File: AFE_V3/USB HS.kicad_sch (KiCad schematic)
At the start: 29 parts, among them IC16 USB3300-EZK-TR, IC17 STMPS2151MTR, J2 USB_C_Receptacle_USB2.0_16P, U8 USBLC6-2SC6, Y1 Crystal_GND24

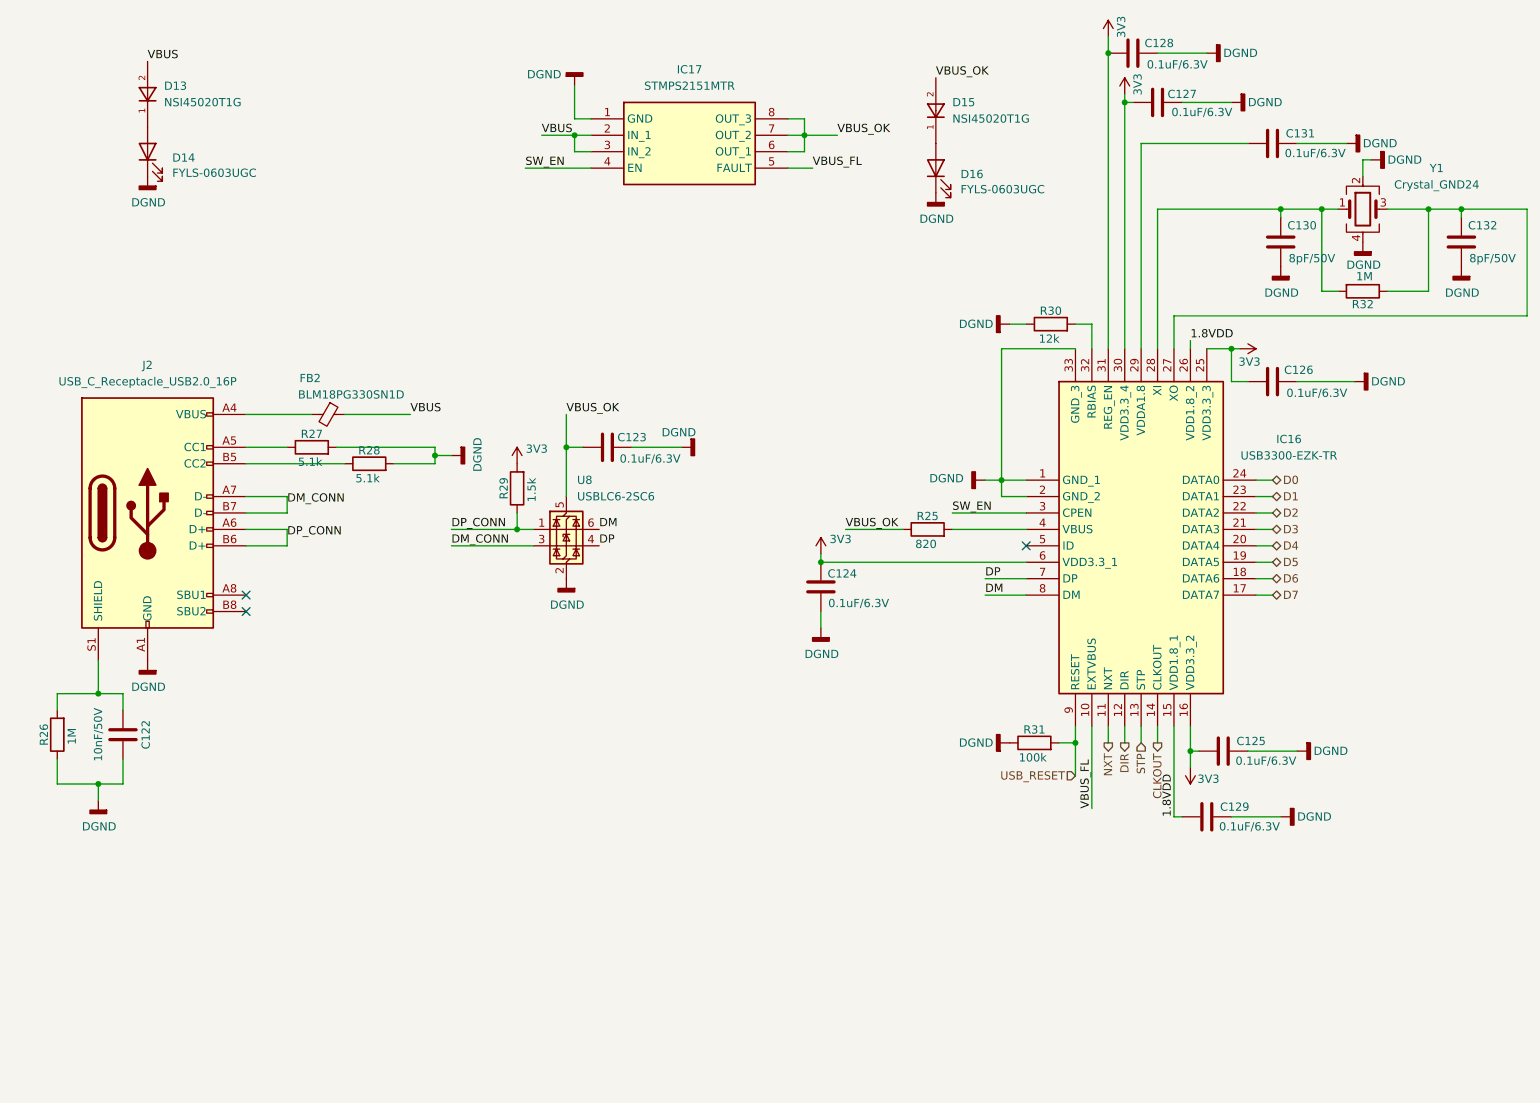
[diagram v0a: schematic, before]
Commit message: PCB tracing in progress. Added some 3d models
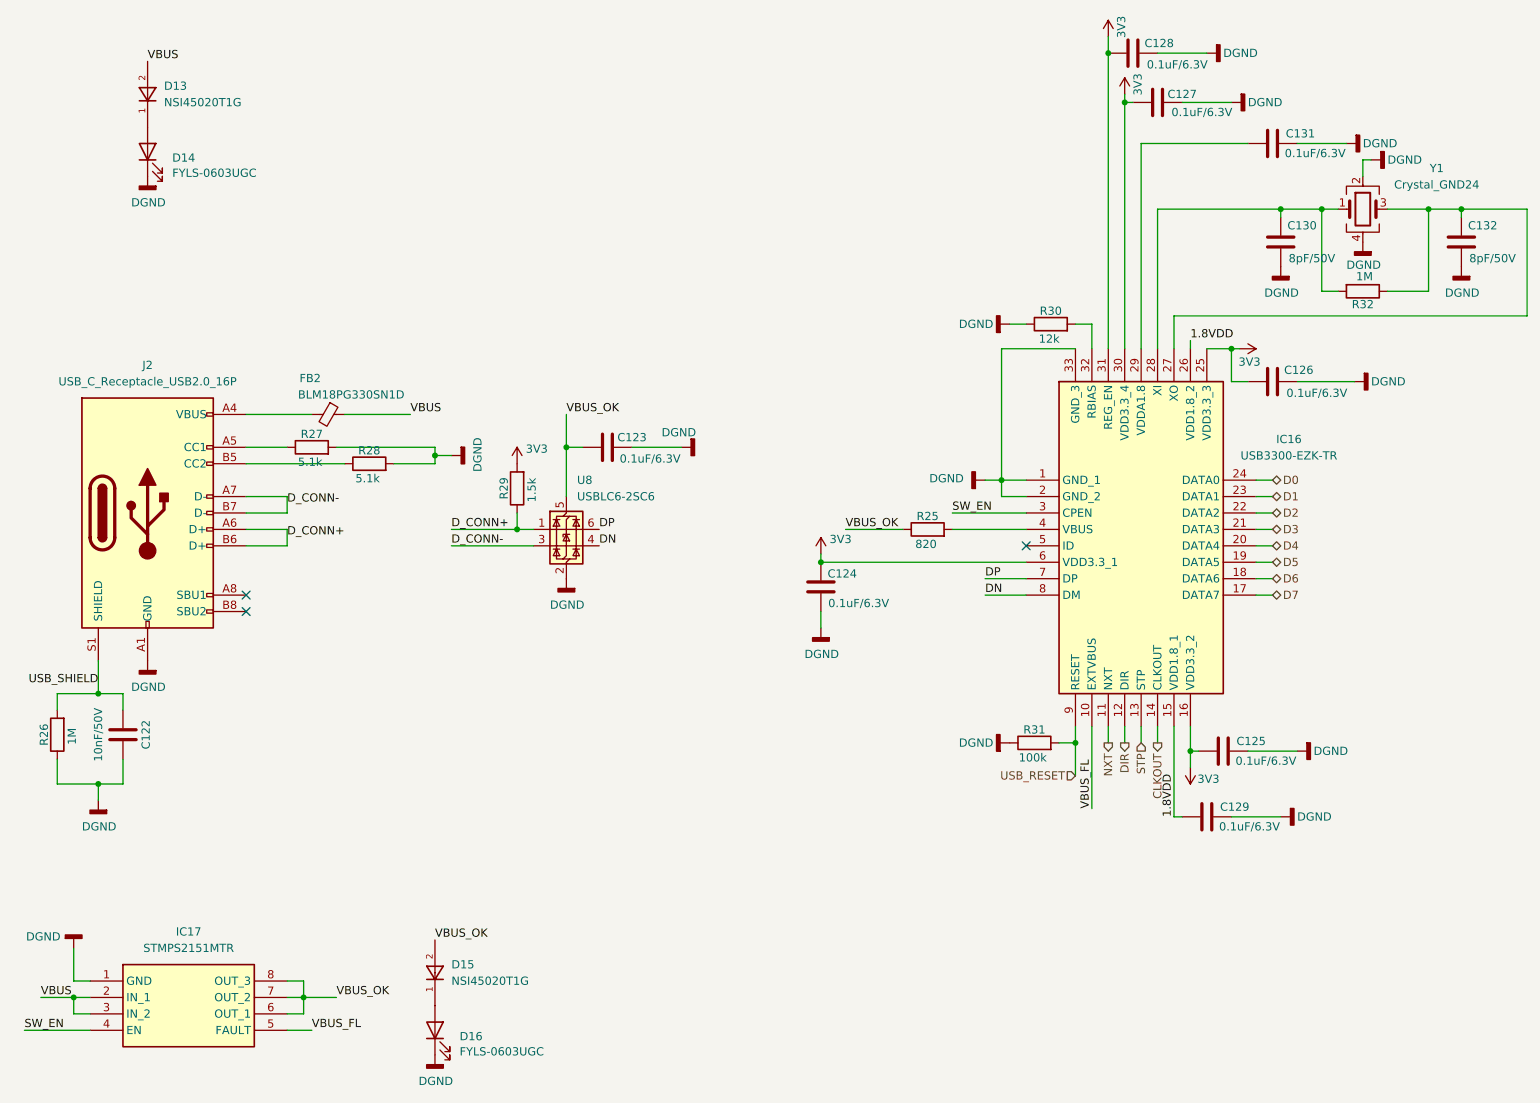
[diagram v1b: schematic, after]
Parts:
- IC16: footprint QFN50P500X500X100-33N-D -> zpc-lib:QFN50P500X500X100-33N-D
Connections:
- net DP: now also U8.6 (I/O1); no longer U8.4 (I/O2)
- net USB_SHIELD: now reaches C122.1, J2.S1 (SHIELD), R26.2
- net DM renamed DN
- net DN: now also U8.4 (I/O2); no longer U8.6 (I/O1)
- net DM_CONN renamed D_CONN-
- net DP_CONN renamed D_CONN+
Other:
- moved on the sheet: D15, D16, IC17

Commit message: PCB tracing in progress
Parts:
- added C53: 0.1uF/6.3V, Capacitor_SMD:C_0603_1608Metric_Pad1.08x0.95mm_HandSolder, symbol Device:C
- IC16: footprint zpc-lib:QFN50P500X500X100-33N-D -> QFN50P500X500X100-33N-D
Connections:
- net DGND: now also C53.2
- net 1.8VDD: no longer names the net of C129.1, IC16.15 (VDD1.8_1)
- net 1.8VDD: no longer IC16.26 (VDD1.8_2)
- new net: C53.1, IC16.26 (VDD1.8_2)
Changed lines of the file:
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@@
 	(wire
 		(pts
-			(xy 199.39 71.12) (xy 199.39 72.39)
+			(xy 199.39 69.85) (xy 199.39 72.39)
 		)
 		(stroke
@@
 	(wire
 		(pts
+			(xy 218.44 69.85) (xy 226.06 69.85)
+		)
+		(stroke
+			(width 0)
+			(type default)
+		)
+	)
+	(wire
+		(pts
 			(xy 186.69 133.35) (xy 186.69 130.81)
 		)
@@
 	(wire
 		(pts
+			(xy 210.82 69.85) (xy 199.39 69.85)
+		)
+		(stroke
+			(width 0)
+			(type default)
+		)
+	)
+	(wire
+		(pts
 			(xy 162.56 100.33) (xy 173.99 100.33)
 		)
@@
 		)
 	)
-	(label "1.8VDD"
-		(at 196.85 144.78 90)
-		(fields_autoplaced yes)
-		(effects
-			(font
-				(size 1.27 1.27)
-			)
-			(justify left bottom)
-		)
-	)
 	(label "VBUS_FL"
 		(at 63.5 177.8 0)
@@
 		)
 	)
-	(label "1.8VDD"
-		(at 199.39 71.12 0)
-		(fields_autoplaced yes)
-		(effects
-			(font
-				(size 1.27 1.27)
-			)
-			(justify left bottom)
-		)
-	)
 	(label "VBUS_FL"
 		(at 184.15 143.51 90)
@@
 			)
 		)
-		(property "Footprint" "zpc-lib:QFN50P500X500X100-33N-D"
+		(property "Footprint" "QFN50P500X500X100-33N-D"
 			(at 205.74 174.93 0)
 			(effects
@@
 	)
 	(symbol
+		(lib_id "Device:C")
+		(at 214.63 69.85 90)
+		(mirror x)
+		(unit 1)
+		(exclude_from_sim no)
+		(in_bom yes)
+		(on_board yes)
+		(dnp no)
+		(property "Reference" "C53"
+			(at 218.948 68.326 90)
+			(effects
+				(font
+					(size 1.27 1.27)
+				)
+			)
+		)
+		(property "Value" "0.1uF/6.3V"
+			(at 221.234 71.374 90)
+			(effects
+				(font
+					(size 1.27 1.27)
+				)
+			)
+		)
+		(property "Footprint" "Capacitor_SMD:C_0603_1608Metric_Pad1.08x0.95mm_HandSolder"
+			(at 218.44 70.8152 0)
+			(effects
+				(font
+					(size 1.27 1.27)
+				)
+				(hide yes)
+			)
+		)
+		(property "Datasheet" "~"
+			(at 214.63 69.85 0)
+			(effects
+				(font
+					(size 1.27 1.27)
+				)
+				(hide yes)
+			)
+		)
+		(property "Description" "Unpolarized capacitor"
+			(at 214.63 69.85 0)
+			(effects
+				(font
+					(size 1.27 1.27)
+				)
+				(hide yes)
+			)
+		)
+		(pin "2"
+		)
+		(pin "1"
+		)
+		(instances
+			(project "AFE_V3"
+				(path "/e9ffbb94-33e2-4158-ac4a-a33b17b122cf/cf962eaa-adb1-4d3a-b0f1-52da2b2e3e19"
+					(reference "C53")
+					(unit 1)
+				)
+			)
+		)
+	)
+	(symbol
 		(lib_id "power:GNDD")
 		(at 224.79 77.47 90)
@@
 					(unit 1)
 				)
+			)
+		)
+	)
+	(symbol
+		(lib_id "power:GNDD")
+		(at 226.06 69.85 90)
+		(mirror x)
+		(unit 1)
+		(exclude_from_sim no)
+		(in_bom yes)
+		(on_board yes)
+		(dnp no)
+		(property "Reference" "#PWR085"
+			(at 232.41 69.85 0)
+			(effects
+				(font
+					(size 1.27 1.27)
+				)
+				(hide yes)
+			)
+		)
+		(property "Value" "DGND"
+			(at 228.6 69.85 90)
+			(effects
+				(font
+					(size 1.27 1.27)
+				)
+				(justify right)
+			)
+		)
+		(property "Footprint" ""
+			(at 226.06 69.85 0)
+			(effects
+				(font
+					(size 1.27 1.27)
+				)
+				(hide yes)
+			)
+		)
+		(property "Datasheet" ""
+			(at 226.06 69.85 0)
+			(effects
+				(font
+					(size 1.27 1.27)
+				)
+				(hide yes)
+			)
+		)
+		(property "Description" "Power symbol creates a global label with name \"GNDD\" , digital ground"
+			(at 226.06 69.85 0)
+			(effects
+				(font
+					(size 1.27 1.27)
+				)
+				(hide yes)
+			)
+		)
+		(pin "1"
+		)
+		(instances
+			(project "AFE_V3"
+				(path "/e9ffbb94-33e2-4158-ac4a-a33b17b122cf/cf962eaa-adb1-4d3a-b0f1-52da2b2e3e19"
+					(reference "#PWR085")
+					(unit 1)
+				)
